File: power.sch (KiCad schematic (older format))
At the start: 57 parts, among them J12 Barrel_Jack_Switch, J13 Conn_02x05_Odd_Even, J14 Screw_Terminal_01x12, U13 LT3471, U14 LP38692MP-5.0, U15 LP38693MP-3.3, U16 LM2937xMP, U17 MAX6070BAUT21+T, U18 LP38693MP-1.8, U19 MC79M15_TO252, U20 LP38693MP-2.5

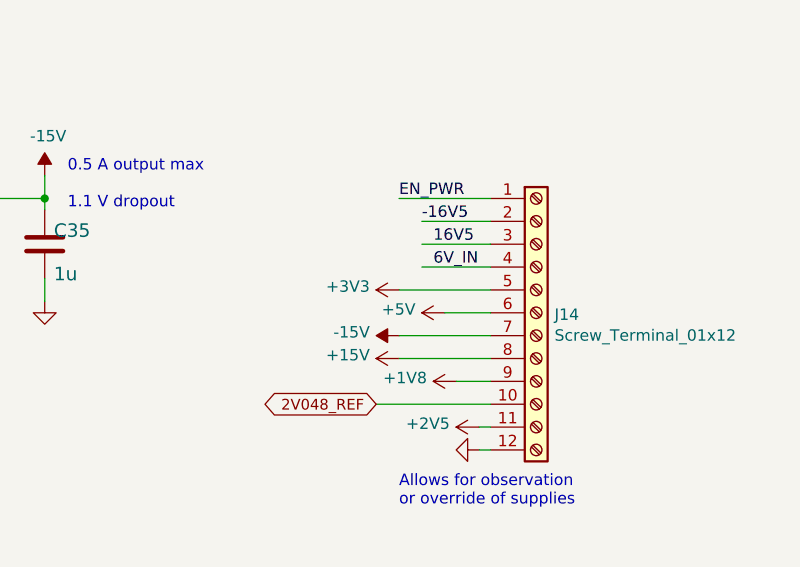
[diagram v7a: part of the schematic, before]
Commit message: moved adc pins around
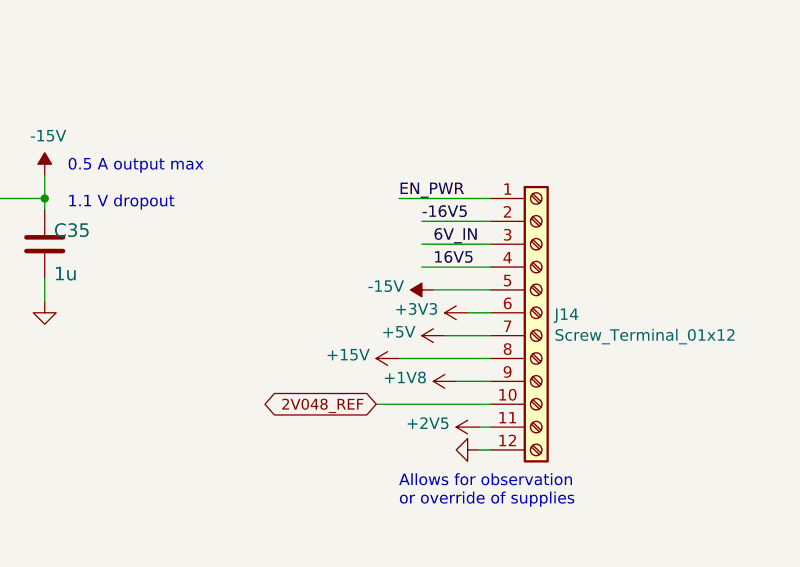
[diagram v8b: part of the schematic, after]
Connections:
- net +3V3: now also J14.6 (Pin_6); no longer J14.5 (Pin_5)
- net +5V: now also J14.7 (Pin_7); no longer J14.6 (Pin_6)
- net -15V: now also J14.5 (Pin_5); no longer J14.7 (Pin_7)
- net 16V5: now also J14.4 (Pin_4); no longer J14.3 (Pin_3)
- net 6V_IN: now also J14.3 (Pin_3); no longer J14.4 (Pin_4)
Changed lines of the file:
@@
 L power:-15V #PWR072
 U 1 1 61216E43
-P 11100 4750
-F 0 "#PWR072" H 11100 4850 50  0001 C CNN
-F 1 "-15V" V 11115 4878 50  0000 L CNN
-F 2 "" H 11100 4750 50  0001 C CNN
-F 3 "" H 11100 4750 50  0001 C CNN
-	1    11100 4750
+P 11250 4550
+F 0 "#PWR072" H 11250 4650 50  0001 C CNN
+F 1 "-15V" V 11265 4678 50  0000 L CNN
+F 2 "" H 11250 4550 50  0001 C CNN
+F 3 "" H 11250 4550 50  0001 C CNN
+	1    11250 4550
 	0    -1   -1   0
 $EndComp
@@
 L power:+3V3 #PWR071
 U 1 1 61217D14
-P 11100 4550
-F 0 "#PWR071" H 11100 4400 50  0001 C CNN
-F 1 "+3V3" V 11115 4678 50  0000 L CNN
-F 2 "" H 11100 4550 50  0001 C CNN
-F 3 "" H 11100 4550 50  0001 C CNN
-	1    11100 4550
+P 11400 4650
+F 0 "#PWR071" H 11400 4500 50  0001 C CNN
+F 1 "+3V3" V 11415 4778 50  0000 L CNN
+F 2 "" H 11400 4650 50  0001 C CNN
+F 3 "" H 11400 4650 50  0001 C CNN
+	1    11400 4650
 	0    -1   -1   0
 $EndComp
@@
 L power:+5V #PWR074
 U 1 1 612190C3
-P 11300 4650
-F 0 "#PWR074" H 11300 4500 50  0001 C CNN
-F 1 "+5V" V 11315 4778 50  0000 L CNN
-F 2 "" H 11300 4650 50  0001 C CNN
-F 3 "" H 11300 4650 50  0001 C CNN
-	1    11300 4650
+P 11300 4750
+F 0 "#PWR074" H 11300 4600 50  0001 C CNN
+F 1 "+5V" V 11315 4878 50  0000 L CNN
+F 2 "" H 11300 4750 50  0001 C CNN
+F 3 "" H 11300 4750 50  0001 C CNN
+	1    11300 4750
 	0    -1   -1   0
 $EndComp
@@
 Text Label 11200 4250 0    50   ~ 0
 -16V5
+Text Label 11250 4450 0    50   ~ 0
+16V5
 Text Label 11250 4350 0    50   ~ 0
-16V5
-Text Label 11250 4450 0    50   ~ 0
 6V_IN
 Text Notes 11100 5500 0    50   ~ 0
@@
 	7000 5600 7000 5550
 Wire Wire Line
-	11500 4650 11300 4650
-Wire Wire Line
-	11500 4550 11100 4550
-Wire Wire Line
 	11500 5150 11450 5150
 Wire Wire Line
@@
 	6400 5300 6400 5500
 Wire Wire Line
-	11100 4750 11500 4750
+	11300 4750 11500 4750
 Wire Wire Line
 	2700 3750 2700 3650
@@
 $EndComp
 $Comp
-L power:GND #GND?
+L power:GND #GND0280
 U 1 1 60FF305F
 P 11450 5250
-F 0 "#GND?" H 11450 5250 50  0001 C CNN
+F 0 "#GND0280" H 11450 5250 50  0001 C CNN
 F 1 "GND" H 11350 5150 59  0001 L BNN
 F 2 "" H 11450 5250 50  0001 C CNN
@@
 Wire Wire Line
 	11100 4150 11500 4150
+Wire Wire Line
+	11400 4650 11500 4650
+Wire Wire Line
+	11250 4550 11500 4550
 $EndSCHEMATC
